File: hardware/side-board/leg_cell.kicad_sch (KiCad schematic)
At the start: 7 parts, among them IC1 STM32C092KCT6, IC2 TCAN332DR, IC3 TPS56A37RPAR, IC4 INA181A1IDBVR

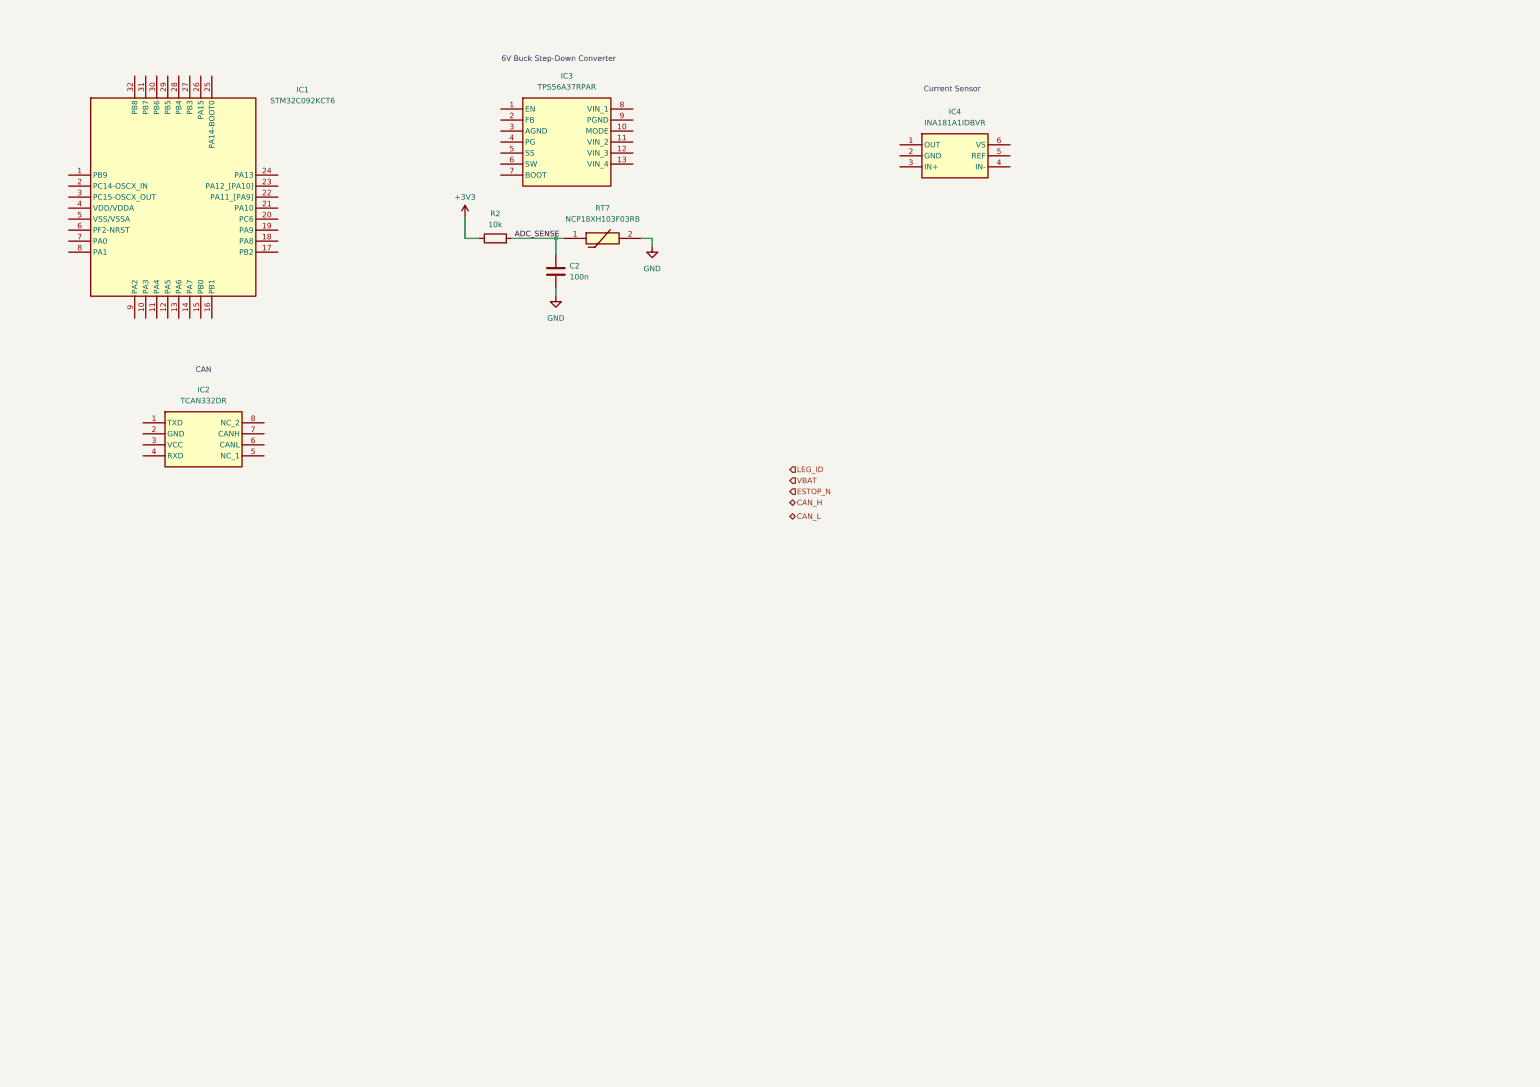
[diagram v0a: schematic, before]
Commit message: Added leg configuration bits
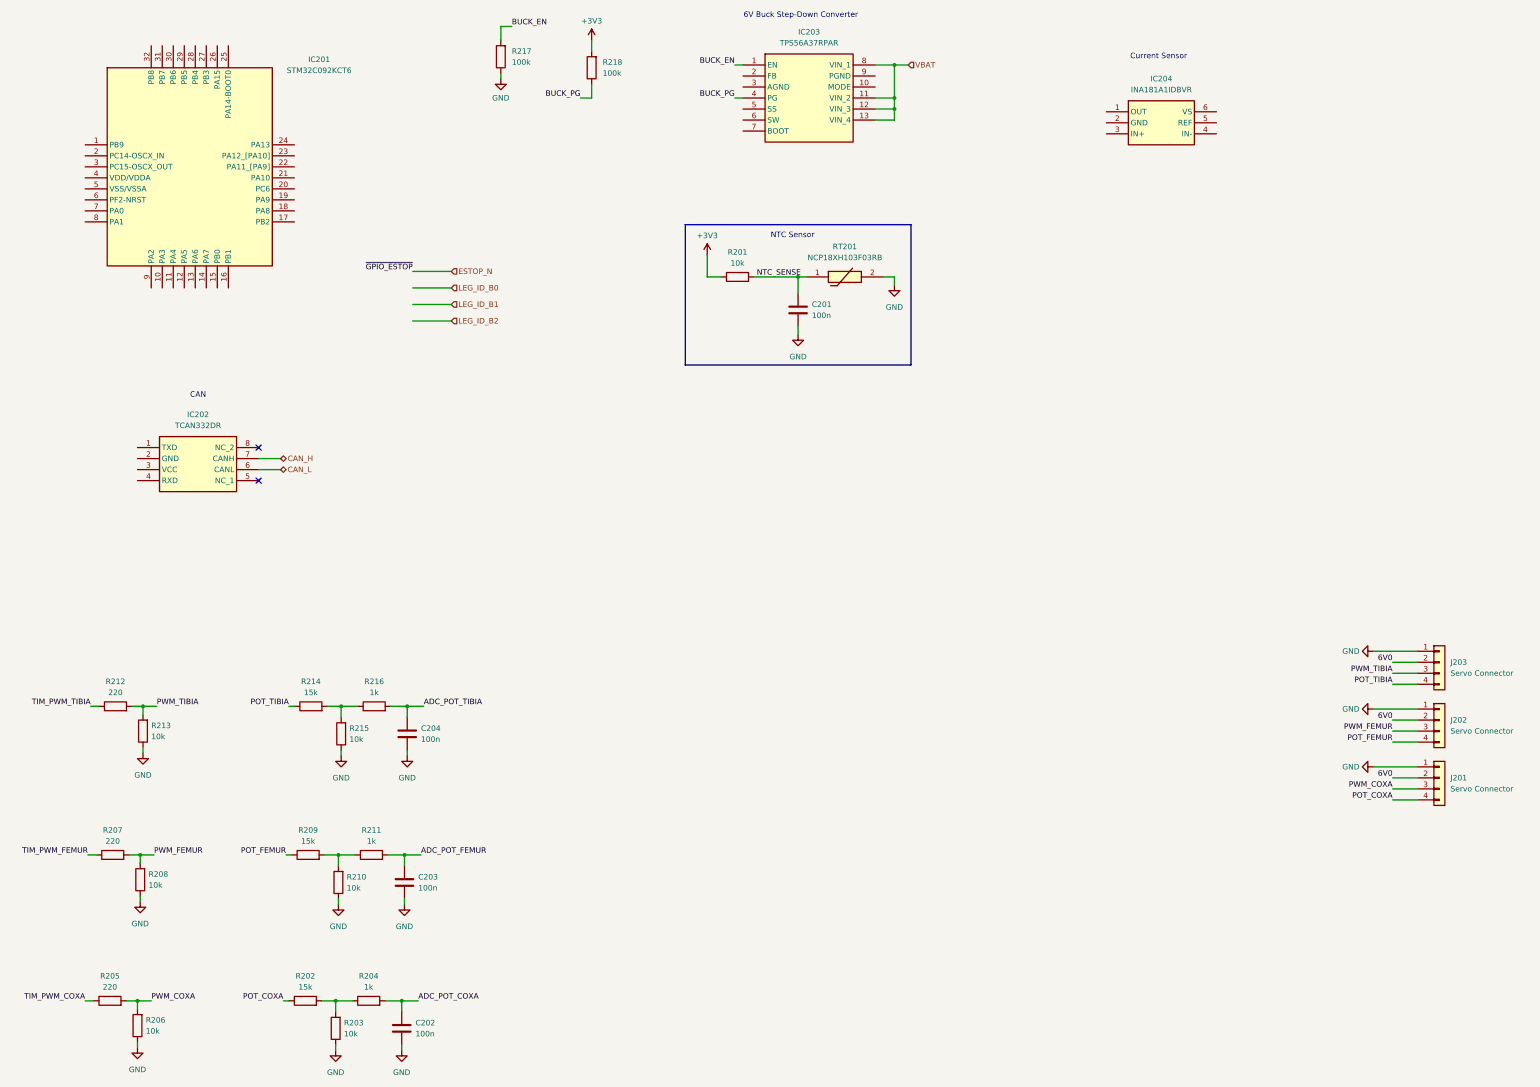
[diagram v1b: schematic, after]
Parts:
- added C202, C203, C204: 100n, Capacitor_SMD:C_0603_1608Metric, symbol Device:C
- added J201, J202, J203: Servo Connector, Connector_JST:JST_XH_S4B-XH-A-1_1x04_P2.50mm_Horizontal, symbol Connector_Generic:Conn_01x04
- added R202, R209, R214: 15k, Resistor_SMD:R_0603_1608Metric, symbol Device:R
- added R203, R206, R208, R210, R213, R215: 10k, Resistor_SMD:R_0603_1608Metric, symbol Device:R
- added R204, R211, R216: 1k, Resistor_SMD:R_0603_1608Metric, symbol Device:R
- added R205, R207, R212: 220, Resistor_SMD:R_0603_1608Metric, symbol Device:R
- added R217, R218: 100k, Resistor_SMD:R_0603_1608Metric, symbol Device:R
- renumbered C2 to C201, IC1 to IC201, IC2 to IC202, IC3 to IC203, IC4 to IC204, R2 to R201, RT7 to RT201
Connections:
- net +3V3: now also R218.2
- net CAN_H: now also IC202.7 (CANH)
- net CAN_L: now also IC202.6 (CANL)
- net GND: now also C202.2, C203.2, C204.2, J201.1 (Pin_1), J202.1 (Pin_1), J203.1 (Pin_1), R203.1, R206.1, R208.1, R210.1, R213.1, R215.1, R217.1
- net VBAT: now also IC203.11 (VIN_2), IC203.12 (VIN_3), IC203.13 (VIN_4), IC203.8 (VIN_1)
- net BUCK_EN: now reaches IC203.1 (EN)
- net BUCK_EN: now also R217.2
- net BUCK_PG: now reaches IC203.4 (PG)
- net BUCK_PG: now also R218.1
- net ADC_SENSE renamed NTC_SENSE
- new net: R202.2, R203.2, R204.1
- new net: R209.2, R210.2, R211.1
- new net: R214.2, R215.2, R216.1
- new net 6V0: J201.2 (Pin_2), J202.2 (Pin_2), J203.2 (Pin_2)
- new net ADC_POT_COXA: C202.1, R204.2
- new net ADC_POT_FEMUR: C203.1, R211.2
- new net ADC_POT_TIBIA: C204.1, R216.2
- new net POT_COXA: J201.4 (Pin_4), R202.1
- new net POT_FEMUR: J202.4 (Pin_4), R209.1
- new net POT_TIBIA: J203.4 (Pin_4), R214.1
- new net PWM_COXA: J201.3 (Pin_3), R205.2, R206.2
- new net PWM_FEMUR: J202.3 (Pin_3), R207.2, R208.2
- new net PWM_TIBIA: J203.3 (Pin_3), R212.2, R213.2
- new net TIM_PWM_COXA: R205.1
- new net TIM_PWM_FEMUR: R207.1
- new net TIM_PWM_TIBIA: R212.1
- no-connect marks 0 -> 2
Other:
- note added: "NTC Sensor"
- moved on the sheet: C201, IC201, IC202, IC203, IC204, R201, RT201

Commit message: Added more leg firmware features
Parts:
- added C205: 100n, Capacitor_SMD:C_0805_2012Metric, symbol Device:C
- added D201: RED, LED_SMD:LED_0805_2012Metric, symbol Device:LED
- added D202: GREEN, LED_SMD:LED_0805_2012Metric, symbol Device:LED
- added J204: TC2050, Connector:Tag-Connect_TC2050-IDC-FP_2x05_P1.27mm_Vertical, symbol Connector:TC2050
- added J205: Conn_01x06, Connector_JST:JST_XH_B6B-XH-A_1x06_P2.50mm_Vertical, symbol Connector_Generic:Conn_01x06
- added R219, R220: 1k, Resistor_SMD:R_0603_1608Metric, symbol Device:R
- added R221: 100k, Resistor_SMD:R_0603_1608Metric, symbol Device:R
- added TP201: DBG, TestPoint:TestPoint_Pad_D2.0mm, symbol Connector:TestPoint
- added TP202: GND, TestPoint:TestPoint_Pad_D2.0mm, symbol Connector:TestPoint
- added TP203: 3V3, TestPoint:TestPoint_Pad_D2.0mm, symbol Connector:TestPoint
- added TP204: 6V0, TestPoint:TestPoint_Pad_D2.0mm, symbol Connector:TestPoint
- added TP205: VBAT, TestPoint:TestPoint_Pad_D2.0mm, symbol Connector:TestPoint
- added TP206: POT_FEMUR, TestPoint:TestPoint_Pad_D2.0mm, symbol Connector:TestPoint
- added TP207: POT_COXA, TestPoint:TestPoint_Pad_D2.0mm, symbol Connector:TestPoint
- added TP208: POT_TIBIA, TestPoint:TestPoint_Pad_D2.0mm, symbol Connector:TestPoint
- added TP209: PWM_TIBIA, TestPoint:TestPoint_Pad_D2.0mm, symbol Connector:TestPoint
- added TP210: PWM_FEMUR, TestPoint:TestPoint_Pad_D2.0mm, symbol Connector:TestPoint
- added TP211: PWM_COXA, TestPoint:TestPoint_Pad_D2.0mm, symbol Connector:TestPoint
- added TP212: I_LEG, TestPoint:TestPoint_Pad_D2.0mm, symbol Connector:TestPoint
- added TP213: BUCK_EN, TestPoint:TestPoint_Pad_D2.0mm, symbol Connector:TestPoint
- added TP214: BUCK_PG, TestPoint:TestPoint_Pad_D2.0mm, symbol Connector:TestPoint
- R202, R209, R214: value 15k -> 10k
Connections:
- net +3V3: now also IC201.4 (VDD/VDDA), IC202.3 (VCC), J204.1, J205.1 (Pin_1), R221.2, TP203.1
- net 6V0: now also R219.2, TP204.1
- net BUCK_EN: now also TP213.1
- net BUCK_PG: now also TP214.1
- net GND: now also IC201.5 (VSS/VSSA), IC202.2 (GND), C205.1, D201.1 (K), D202.1 (K), J204.3, J204.5, J204.9, J205.2 (Pin_2), TP202.1
- net LEG_ID_B0: now also IC201.27 (PB3)
- net LEG_ID_B1: now also IC201.32 (PB8)
- net LEG_ID_B2: now also IC201.1 (PB9)
- net POT_COXA: now also TP207.1
- net POT_FEMUR: now also TP206.1
- net POT_TIBIA: now also TP208.1
- net PWM_COXA: now also TP211.1
- net PWM_FEMUR: now also TP210.1
- net PWM_TIBIA: now also TP209.1
- net VBAT: now also TP205.1
- net PA7: now reaches IC201.14 (PA7)
- net PA7: now also TP201.1
- net ~{ESTOP}: now reaches IC201.17 (PB2)
- net ~{ESTOP}: now also R221.1
- net SWDIO: now reaches IC201.24 (PA13)
- net SWDIO: now also J204.2
- net BOOT0: now reaches IC201.25 (PA14-BOOT0)
- net BOOT0: now also J204.4
- net PA15: now reaches IC201.26 (PA15)
- net PA15: now also R220.2
- net TOF_INT: now reaches IC201.28 (PB4)
- net TOF_INT: now also J205.5 (Pin_5)
- net TOF_SHUT: now reaches IC201.29 (PB5)
- net TOF_SHUT: now also J205.6 (Pin_6)
- net I2C_SCL: now reaches IC201.30 (PB6)
- net I2C_SCL: now also J205.4 (Pin_4)
- net I2C_SDA: now reaches IC201.31 (PB7)
- net I2C_SDA: now also J205.3 (Pin_3)
- net NRST: now reaches IC201.6 (PF2-NRST)
- net NRST: now also C205.2, J204.10
- new net: D202.2 (A), R220.1
- new net: D201.2 (A), R219.1
- no-connect marks 2 -> 5
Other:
- moved on the sheet: C204, J201, J202, R205, R206, R207, R208, R212, R213, R214, R215, R216

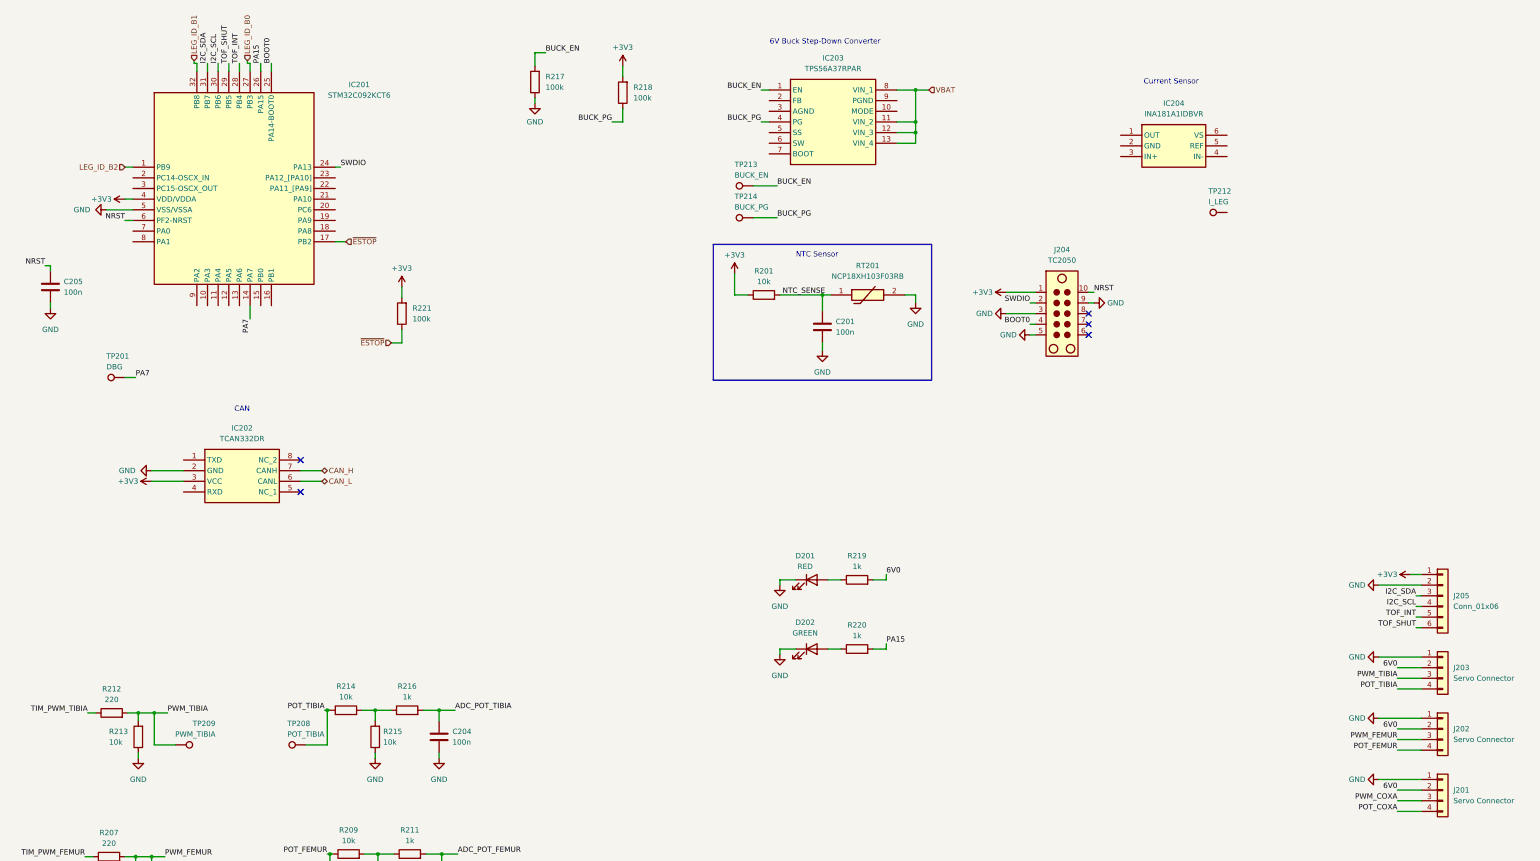
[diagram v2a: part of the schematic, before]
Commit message: Updated schematic circuit for side board
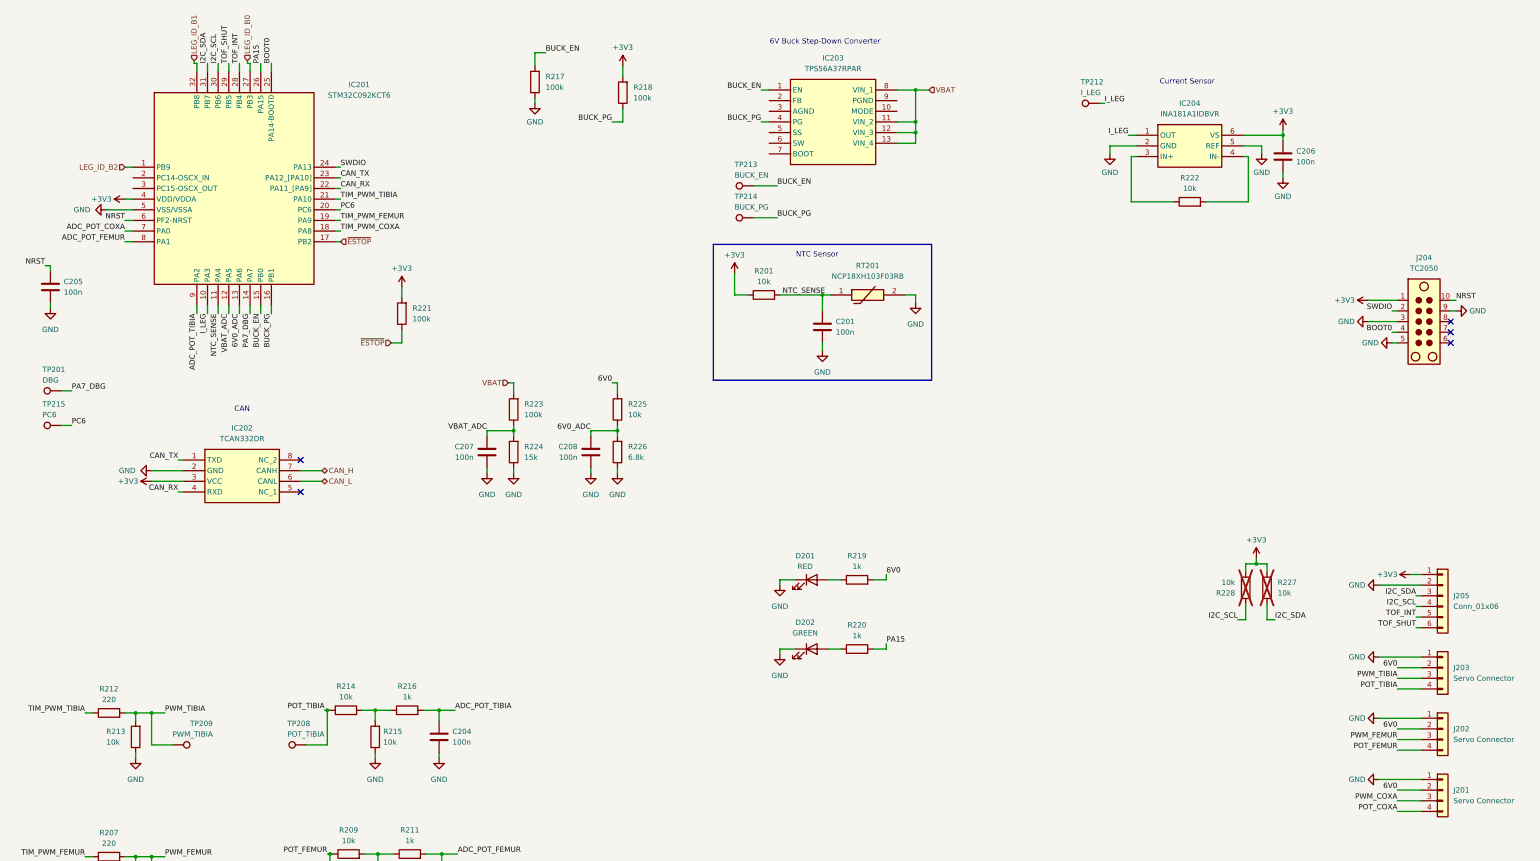
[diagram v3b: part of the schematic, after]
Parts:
- added C206, C207, C208: 100n, Capacitor_SMD:C_0805_2012Metric, symbol Device:C
- added R222, R225, R227, R228: 10k, Resistor_SMD:R_0603_1608Metric, symbol Device:R
- added R223: 100k, Resistor_SMD:R_0603_1608Metric, symbol Device:R
- added R224: 15k, Resistor_SMD:R_0603_1608Metric, symbol Device:R
- added R226: 6.8k, Resistor_SMD:R_0603_1608Metric, symbol Device:R
- added TP215: PC6, TestPoint:TestPoint_Pad_D2.0mm, symbol Connector:TestPoint
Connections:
- net +3V3: now also IC204.6 (VS), C206.2, R227.2, R228.1
- net 6V0: now also R225.2
- net ADC_POT_COXA: now also IC201.7 (PA0)
- net ADC_POT_FEMUR: now also IC201.8 (PA1)
- net ADC_POT_TIBIA: now also IC201.9 (PA2)
- net BUCK_EN: now also IC201.15 (PB0)
- net BUCK_PG: now also IC201.16 (PB1)
- net GND: now also IC204.2 (GND), IC204.5 (REF), C206.1, C207.2, C208.2, R224.1, R226.1
- net I2C_SCL: now also R228.2
- net I2C_SDA: now also R227.1
- net NTC_SENSE: now also IC201.11 (PA4)
- net TIM_PWM_COXA: now also IC201.18 (PA8)
- net TIM_PWM_FEMUR: now also IC201.19 (PA9)
- net TIM_PWM_TIBIA: now also IC201.21 (PA10)
- net VBAT: now also R223.2
- net I_LEG: now reaches TP212.1
- net I_LEG: now also IC201.10 (PA3), IC204.1 (OUT)
- net CAN_TX: now reaches IC202.1 (TXD)
- net CAN_TX: now also IC201.23 (PA12_[PA10])
- net CAN_RX: now reaches IC202.4 (RXD)
- net CAN_RX: now also IC201.22 (PA11_[PA9])
- net at IC204.3 (IN+): now also R222.1
- net at IC204.4 (IN-): now also R222.2
- net VBAT_ADC: now reaches IC201.12 (PA5)
- net VBAT_ADC: now also C207.1, R223.1, R224.2
- net 6V0_ADC: now reaches IC201.13 (PA6)
- net 6V0_ADC: now also C208.1, R225.1, R226.2
- net PC6: now reaches IC201.20 (PC6)
- net PC6: now also TP215.1
- net PA7 renamed PA7_DBG
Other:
- moved on the sheet: IC204, J204, R212, R213, TP201, TP209
